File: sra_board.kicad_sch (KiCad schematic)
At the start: 80 parts, among them J1 Conn_01x14_Pin, J2 Conn_01x14_Pin, J4 Conn_01x04_Pin, U1 MAX7219CWG_T, U2 ESP32-WROOM-32E, U3 TB6612FNG H-bridge Motor Driv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

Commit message: Added OLED, Servo Ports, Power Ports, CH340, Boot circuit, Motor port
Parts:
- removed J3: ~, PCB_USBC:PCBTypeC_14P, symbol PCB_USBC:PCBTypeC_14P
- added C10, C11, C6, C7: 0.1uf, symbol Device:C
- added C4, C5: 1uf, symbol Device:C
- added C8: 0.1uF, Capacitor_SMD:C_0805_2012Metric, symbol ESP32-S2-rescue:C-Device
- added C9: 0.1 uF, Capacitor_SMD:C_0805_2012Metric, symbol Device:C
- added J10, J3, J5, J6, J7, J8, J9: Conn_01x03_Pin, symbol Connector:Conn_01x03_Pin
- added J11: Conn_01x08_Pin, symbol Connector:Conn_01x08_Pin
- added J12: Conn_01x07_Pin, symbol Connector:Conn_01x07_Pin
- added J13: Conn_01x04_Pin, symbol Connector:Conn_01x04_Pin
- added J14, J15: Conn_01x02_Pin, symbol Connector:Conn_01x02_Pin
- added Q1, Q2: SS8050, Package_TO_SOT_SMD:SOT-23, symbol MMBT8050:MMBT8050
- added R10, R5: 10K, Resistor_SMD:R_0805_2012Metric_Pad1.20x1.40mm_HandSolder, symbol ESP32-S2-rescue:R-Device
- added R11, R12: 10k, symbol Device:R
- added R3, R4: R, symbol Device:R
- added SW3: SW_IO0, Button_Switch_SMD:SW_Push_SPST_NO_Alps_SKRK, symbol ESP32-S2-rescue:SW_Push-Switch
- added SW5: SW_EN, Button_Switch_SMD:SW_Push_SPST_NO_Alps_SKRK, symbol ESP32-S2-rescue:SW_Push-Switch
- added U4: ME6211C33M5, Package_TO_SOT_SMD:SOT-23-5, symbol Regulator_Linear:ME6211C33M5
- added U5: CH340C, Package_SO:SOIC-16_3.9x9.9mm_P1.27mm, symbol ESP32-S2-rescue:CH340C-Interface_USB
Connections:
- net CLK is gone; now on net 18: U1.13 (CLK), U2.30 (IO18)
- net CS is gone; now on net 5: U1.12 (LOAD), U2.29 (IO5)
- net Din is gone; now on net 23: U1.1 (DIN), U2.37 (IO23)
- net 15: now also J5.1 (Pin_1)
- net 19: now also J6.1 (Pin_1)
- net 21: now also J11.3 (Pin_3), J13.4 (Pin_4), R3.2
- net 22: now also J11.4 (Pin_4), J13.3 (Pin_3), R4.2
- net 27: now also J3.1 (Pin_1)
- net 32: now also J12.1 (Pin_1)
- net 33: now also J7.1 (Pin_1)
- net 34: now also J12.3 (Pin_3)
- net 35: now also J12.2 (Pin_2)
- net 36: now also J12.5 (Pin_5)
- net 39: now also J12.4 (Pin_4)
- net 3V3: now also C5.1, C9.1, J11.1 (Pin_1), J12.7 (Pin_7), J13.2 (Pin_2), J9.1 (Pin_1), J9.2 (Pin_2), J9.3 (Pin_3), R11.2, R12.2, R3.1, R4.1, U4.5 (V_{OUT}), U5.16 (VCC)
- net EN: now also C11.2, Q1.3, R11.1, SW5.2
- net GND: now also C10.1, C11.1, C4.2, C5.2, C8.2, C9.2, J10.1 (Pin_1), J10.2 (Pin_2), J10.3 (Pin_3), J11.2 (Pin_2), J12.6 (Pin_6), J13.1 (Pin_1), J3.3 (Pin_3), J5.3 (Pin_3), J6.3 (Pin_3), J7.3 (Pin_3), SW3.1, SW5.1, U4.2 (V_{SS}), U5.1 (GND)
- net IO0: now also C10.2, Q2.3, R12.1, SW3.2
- net M1A: now also C6.1, J14.1 (Pin_1)
- net M1B: now also C6.2, J14.2 (Pin_2)
- net M2A: now also C7.1, J15.1 (Pin_1)
- net M2B: now also C7.2, J15.2 (Pin_2)
- net RXD: now also U5.2 (TXD)
- net TXD: now also U5.3 (RXD)
- new net: C8.1, U5.4 (V3)
- new net: Q2.1, R10.2
- new net: Q1.1, R5.2
- new net 5V_P: C4.1, J3.2 (Pin_2), J5.2 (Pin_2), J6.2 (Pin_2), J7.2 (Pin_2), J8.1 (Pin_1), J8.2 (Pin_2), J8.3 (Pin_3), U4.1 (V_{IN}), U4.3 (CE)
- new net D+: U5.5 (UD+)
- new net D-: U5.6 (UD-)
- new net ~{DTR}: Q2.2, R5.1, U5.13 (~{DTR})
- new net ~{RTS}: Q1.2, R10.1, U5.14 (~{RTS})
- no-connect marks 0 -> 9
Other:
- note added: "5V->3V3 LDO"
- note added: "Boot switches"
- note added: "CH340 (USB to TTL)"
- note added: "ESP Headers"
- note added: "LSA"
- note added: "MPU-6050"
- note added: "Motor Ports"
- note added: "OLED"
- note added: "Power Ports"
- note added: "Serial Boot"
- note added: "Servo Ports"
- moved on the sheet: J4

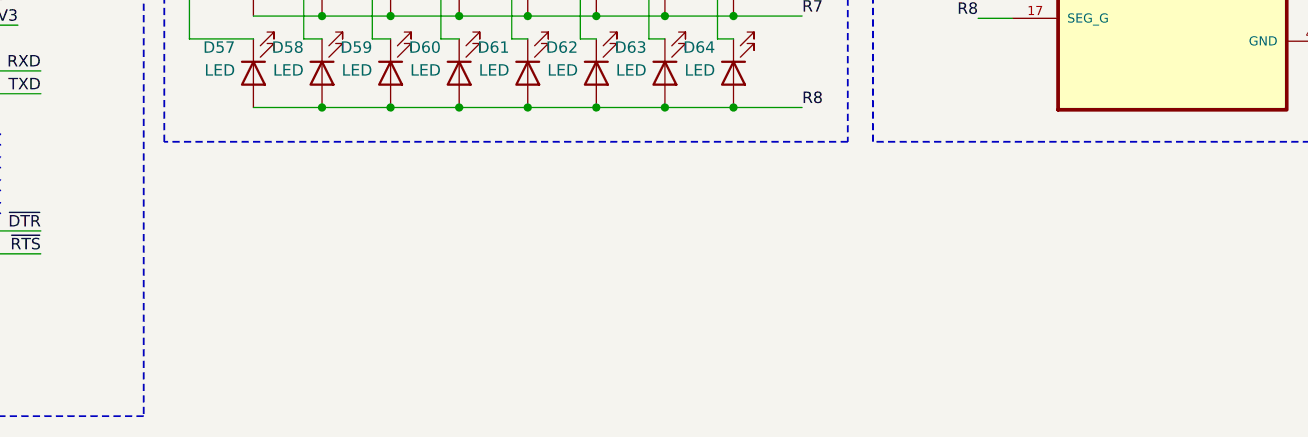
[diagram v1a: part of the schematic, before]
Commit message: Added CN3302 and TCP
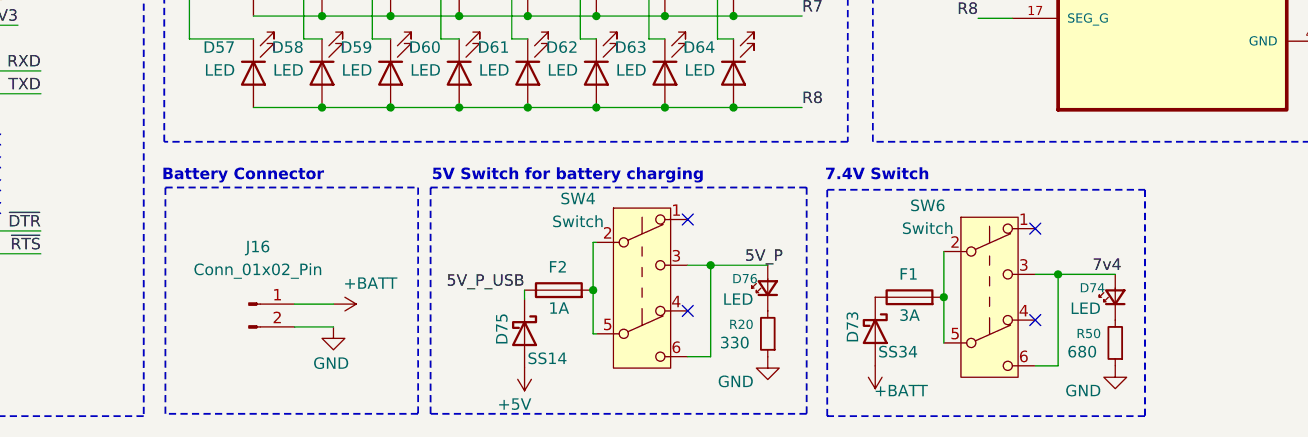
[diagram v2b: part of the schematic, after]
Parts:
- added D73: SS34, Diode_SMD:D_SMB, symbol Diode:1N5822
- added D74, D76: LED, LED_SMD:LED_0603_1608Metric_Pad1.05x0.95mm_HandSolder, symbol Device:LED_Small
- added D75: SS14, Diode_SMD:D_SMA, symbol Diode:1N5822
- added F1: 3A, Fuse:Fuse_Littelfuse-LVR100, symbol Device:Fuse
- added F2: 1A, Fuse:Fuse_Littelfuse-LVR100, symbol Device:Fuse
- added J16: Conn_01x02_Pin, symbol Connector:Conn_01x02_Pin
- added R20: 330, Resistor_SMD:R_0603_1608Metric, symbol Device:R_Small
- added R50: 680, Resistor_SMD:R_0603_1608Metric, symbol Device:R_Small
- added SW4, SW6: Switch, Button_Switch_THT:SW_Push_2P2T_Toggle_CK_PVA2OAH5xxxxxxV2, symbol Switch:SW_Push_DPDT
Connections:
- net 5V_P: now also D76.2 (A), SW4.3 (C), SW4.6 (C)
- net GND: now also J16.2 (Pin_2), R20.1, R50.1
- new net: D76.1 (K), R20.2
- new net: D73.1 (K), F1.1
- new net: F1.2, SW6.2 (B), SW6.5 (B)
- new net: F2.2, SW4.2 (B), SW4.5 (B)
- new net: D74.1 (K), R50.2
- new net +5V: D75.2 (A)
- new net +BATT: D73.2 (A), J16.1 (Pin_1)
- new net 5V_P_USB: D75.1 (K), F2.1
- new net 7v4: D74.2 (A), SW6.3 (C), SW6.6 (C)
- no-connect marks 9 -> 13
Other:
- note added: "5V Switch for battery charging"
- note added: "7.4V Switch"
- note added: "Battery Connector"

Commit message: Added CN3303N circuit
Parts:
- added C12, C13: 10uF, Capacitor_SMD:C_0805_2012Metric, symbol Device:C
- added C14, C16: 0.1uF, Capacitor_SMD:C_0805_2012Metric, symbol Device:C
- added C15: NC, Capacitor_SMD:C_0805_2012Metric, symbol Device:C
- added C17, C18: 22uF, Capacitor_SMD:C_0805_2012Metric, symbol Device:C
- added C21, C22, C23, C24: 22uf, symbol Device:C
- added D65: LED, symbol Device:LED
- added D66: SP0503BAHT, Package_TO_SOT_SMD:SOT-143, symbol Power_Protection:SP0503BAHT
- added D67: GREEN, symbol Device:LED
- added D69, D72: SS34, Diode_SMD:D_SMA, symbol Diode:SS34
- added D70: RED, symbol Device:LED
- added D71: SS14, Diode_SMD:D_SMA, symbol Diode:1N5822
- added H1, H2, H3, H4, H5, H6: MountingHole, symbol Mechanical:MountingHole
- added J17: USB_C_Receptacle_USB2.0_16P, Connector_USB:USB_C_Receptacle_GCT_USB4105-xx-A_16P_TopMnt_Horizontal, symbol Connector:USB_C_Receptacle_USB2.0_16P
- added L1: 3.3uH, symbol Device:L
- added L2: 4.7uH, Inductor_SMD:L_Sunlord_MWSA0402S, symbol Device:L
- added P1: USB_C_Plug_USB2.0, symbol Connector:USB_C_Plug_USB2.0
- added Q3: AO4435, symbol Simulation_SPICE:PMOS
- added Q4: AO4468, symbol Simulation_SPICE:NMOS
- added R13, R15, R23: 220, symbol Device:R
- added R14: 20m, symbol Device:R
- added R17, R18: 10k, Resistor_SMD:R_0805_2012Metric, symbol Device:R_Small
- added R19: 52k3, Resistor_SMD:R_0805_2012Metric, symbol Device:R_Small
- added R21, R22: 5.1K, Resistor_SMD:R_0603_1608Metric, symbol Device:R
- added TP1, TP2, TP3, TP4: TestPoint, symbol Connector:TestPoint
- added U6: TPS562202, Package_TO_SOT_SMD:SOT-563, symbol Regulator_Switching:TPS562202
- added U7: CN3303, easyeda2kicad:SOP-8_L4.9-W3.9-P1.27-LS6.0-BL, symbol easyeda2kicad:CN3302
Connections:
- net 12V_P is gone; now on net 7v4: U3.1 (VM)
- net +5V: now also C15.2, C17.1, C18.1, L2.2, R19.1
- net +BATT: no longer J16.1 (Pin_1)
- net 3V3: now also R13.1
- net 5V: now also TP1.1
- net 5V_P: now also TP2.1
- net 5V_P_USB: now also C21.1, C22.1, D71.1 (K), Q3.3 (S), R14.2, TP4.1, U7.8 (CSN)
- net 7v4: now also C12.1, C13.1, C14.1, R17.1, TP3.1, U6.1 (VIN)
- net D+: now also D66.2 (K), J17.A6 (D+), J17.B6 (D+)
- net D-: now also D66.3 (K), J17.A7 (D-), J17.B7 (D-)
- net GND: now also C12.2, C13.2, C14.2, C17.2, C18.2, C21.2, C22.2, C23.2, C24.2, D65.1 (K), D66.1 (A), D69.2 (A), D70.1 (K), J17.A1 (GND), J17.A12 (GND), J17.B1 (GND), J17.B12 (GND), J17.S1 (SHIELD), Q4.3 (S), R18.1, R21.2, R22.2, U6.3 (GND), U7.4 (GND)
- new net: C16.1, L2.1, U6.2 (SW)
- new net: C16.2, U6.4 (VBST)
- new net: C15.1, R18.2, R19.2, U6.6 (VFB)
- new net: D72.2 (A), L1.2, Q4.1 (D)
- new net: D65.2 (A), R13.2
- new net: D67.2 (A), R15.2
- new net: D67.1 (K), R23.1, U7.1 (STAT)
- new net: D70.2 (A), R23.2
- new net: P1.A1 (GND), P1.A12 (GND), P1.B1 (GND), P1.B12 (GND)
- new net: P1.A4 (VBUS), P1.A9 (VBUS), P1.B4 (VBUS), P1.B9 (VBUS)
- new net: J17.B5 (CC2), R22.1
- new net: D69.1 (K), L1.1, Q3.1 (D)
- new net: R17.2, U6.5 (EN)
- new net: Q4.2 (G), U7.5 (LDRV)
- new net: J17.A5 (CC1), R21.1
- new net BAT: C23.1, C24.1, D72.1 (K), J16.1 (Pin_1), U7.3 (BAT)
- new net HDRV: Q3.2 (G), U7.6 (HDRV)
- new net VBUS: D66.4 (K), D71.2 (A), J17.A4 (VBUS), J17.A9 (VBUS), J17.B4 (VBUS), J17.B9 (VBUS)
- new net VIN: R14.1, R15.1, U7.2 (CE), U7.7 (VIN)
- no-connect marks 13 -> 15
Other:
- note added: "CN3302 (Charging IC)"
- note added: "Mounting Holes"
- note added: "TPS562202 (7.4V->5V)"
- note added: "USB TYPE-C"
- moved on the sheet: C4, C5, U4

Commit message: Fixed net labels
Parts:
- removed D71: SS14, Diode_SMD:D_SMA, symbol Diode:1N5822
- removed P1: USB_C_Plug_USB2.0, symbol Connector:USB_C_Plug_USB2.0
- added D68, D71: SS34, Diode_SMD:D_SMA, symbol Diode:SS34
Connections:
- net +BATT is gone; now on net BAT: D73.2 (A)
- net 5V: no longer TP1.1, U1.19 (V+)
- net 5V_P: now also TP1.1, U1.19 (V+)
- net 5V_P_USB: now also D68.1 (K), D71.1 (K); no longer C21.1, C22.1, Q3.3 (S), R14.2, U7.8 (CSN)
- net 7v4: no longer C12.1, C13.1, C14.1, D74.2 (A), R17.1, SW6.3 (C), SW6.6 (C), U6.1 (VIN)
- net VBUS: now also D68.2 (A)
- new net: C21.1, C22.1, D71.2 (A), Q3.3 (S), R14.2, U7.8 (CSN)
- new net 12V: C12.1, C13.1, C14.1, D74.2 (A), R17.1, SW6.3 (C), SW6.6 (C), U6.1 (VIN)
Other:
- note added: "TPS562202 (12V->5V)"
- note removed: "TPS562202 (7.4V->5V)"

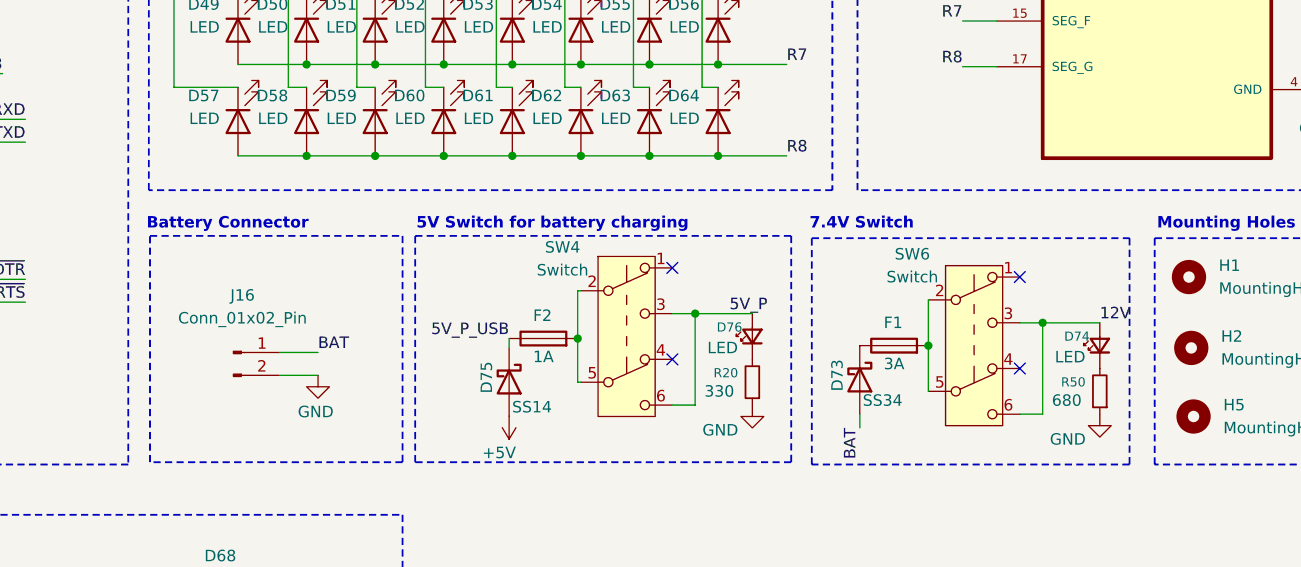
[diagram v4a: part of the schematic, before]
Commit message: fixed text labels
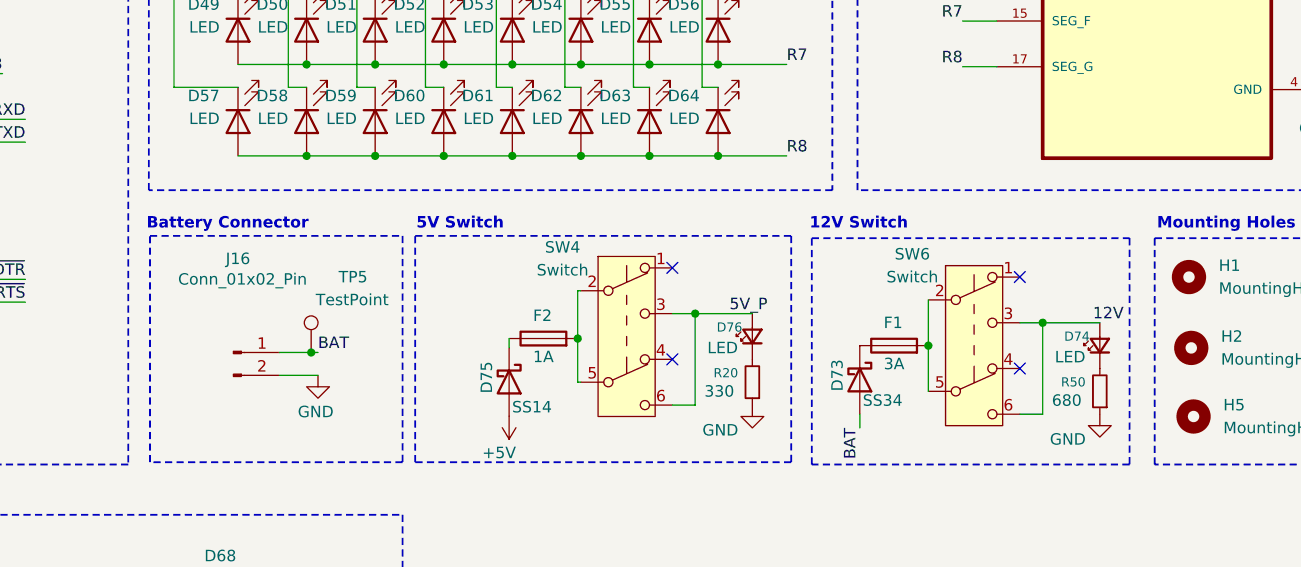
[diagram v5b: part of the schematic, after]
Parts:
- added TP5: TestPoint, symbol Connector:TestPoint
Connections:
- net 5V_P_USB: no longer D75.1 (K), F2.1
- net BAT: now also TP5.1
- new net: D75.1 (K), F2.1
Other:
- note added: "12V Switch"
- note added: "5V Switch"
- note removed: "5V Switch for battery charging"
- note removed: "7.4V Switch"
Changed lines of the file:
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@@
 		)
 	)
-	(text "5V Switch for battery charging\n"
+	(text "5V Switch\n"
 		(exclude_from_sim no)
 		(at 281.178 113.03 0)
@@
 		)
 	)
-	(text "7.4V Switch\n"
+	(text "12V Switch\n"
 		(exclude_from_sim no)
 		(at 324.866 113.03 0)
@@
 	)
 	(junction
+		(at 269.494 127.254)
+		(diameter 0)
+		(color 0 0 0 0)
+	)
+	(junction
 		(at 276.606 85.09)
 		(diameter 0)
@@
 	)
 	(junction
+		(at 350.774 123.952)
+		(diameter 0)
+		(color 0 0 0 0)
+	)
+	(junction
 		(at 268.986 95.25)
 		(diameter 0)
@@
 	)
 	(junction
-		(at 350.774 123.952)
-		(diameter 0)
-		(color 0 0 0 0)
-	)
-	(junction
 		(at 266.954 87.63)
 		(diameter 0)
@@
 	(wire
 		(pts
+			(xy 269.494 127.254) (xy 270.256 127.254)
+		)
+		(stroke
+			(width 0)
+			(type default)
+		)
+	)
+	(wire
+		(pts
 			(xy 150.876 38.1) (xy 155.194 38.1)
 		)
@@
 	(wire
 		(pts
-			(xy 265.938 127.254) (xy 270.256 127.254)
+			(xy 265.938 127.254) (xy 269.494 127.254)
 		)
 		(stroke
@@
 		)
 	)
-	(label "5V_P_USB"
-		(at 291.4904 125.7046 180)
-		(effects
-			(font
-				(size 1.27 1.27)
-			)
-			(justify right bottom)
-		)
-	)
 	(label "21"
 		(at 65.278 65.024 0)
@@
 	)
 	(label "12V"
-		(at 357.124 123.952 0)
+		(at 356.362 123.952 0)
 		(effects
 			(font
@@
 	)
 	(symbol
+		(lib_id "Connector:TestPoint")
+		(at 269.494 127.254 0)
+		(unit 1)
+		(body_style 1)
+		(exclude_from_sim no)
+		(in_bom yes)
+		(on_board yes)
+		(in_pos_files yes)
+		(dnp no)
+		(property "Reference" "TP5"
+			(at 272.542 118.872 0)
+			(show_name no)
+			(do_not_autoplace no)
+			(effects
+				(font
+					(size 1.27 1.27)
+				)
+				(justify left)
+			)
+		)
+		(property "Value" "TestPoint"
+			(at 270.002 121.412 0)
+			(show_name no)
+			(do_not_autoplace no)
+			(effects
+				(font
+					(size 1.27 1.27)
+				)
+				(justify left)
+			)
+		)
+		(property "Footprint" ""
+			(at 274.574 127.254 0)
+			(hide yes)
+			(show_name no)
+			(do_not_autoplace no)
+			(effects
+				(font
+					(size 1.27 1.27)
+				)
+			)
+		)
+		(property "Datasheet" ""
+			(at 274.574 127.254 0)
+			(hide yes)
+			(show_name no)
+			(do_not_autoplace no)
+			(effects
+				(font
+					(size 1.27 1.27)
+				)
+			)
+		)
+		(property "Description" "test point"
+			(at 269.494 127.254 0)
+			(hide yes)
+			(show_name no)
+			(do_not_autoplace no)
+			(effects
+				(font
+					(size 1.27 1.27)
+				)
+			)
+		)
+		(pin "1"
+		)
+		(instances
+			(project "sra_board"
+				(path "/294e2e5f-a7b9-4d81-904c-b55cda9b730c"
+					(reference "TP5")
+					(unit 1)
+				)
+			)
+		)
+	)
+	(symbol
 		(lib_id "Device:Fuse")
 		(at 334.264 126.492 90)
@@
 		(dnp no)
 		(property "Reference" "J16"
-			(at 261.874 120.904 0)
+			(at 261.366 116.84 0)
 			(show_name no)
 			(do_not_autoplace no)
@@
 		)
 		(property "Value" "Conn_01x02_Pin"
-			(at 261.874 123.444 0)
+			(at 261.874 119.126 0)
 			(show_name no)
 			(do_not_autoplace no)
